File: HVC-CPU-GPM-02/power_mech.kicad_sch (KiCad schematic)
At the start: 24 parts, among them P6 POWER, SW1 RESET, U1 MB8416, U2 74LS373, U3 74LS139, U4 MB8416, U5 RP2C02, U6 RP2A03, U7 74LS368, U8 74LS368

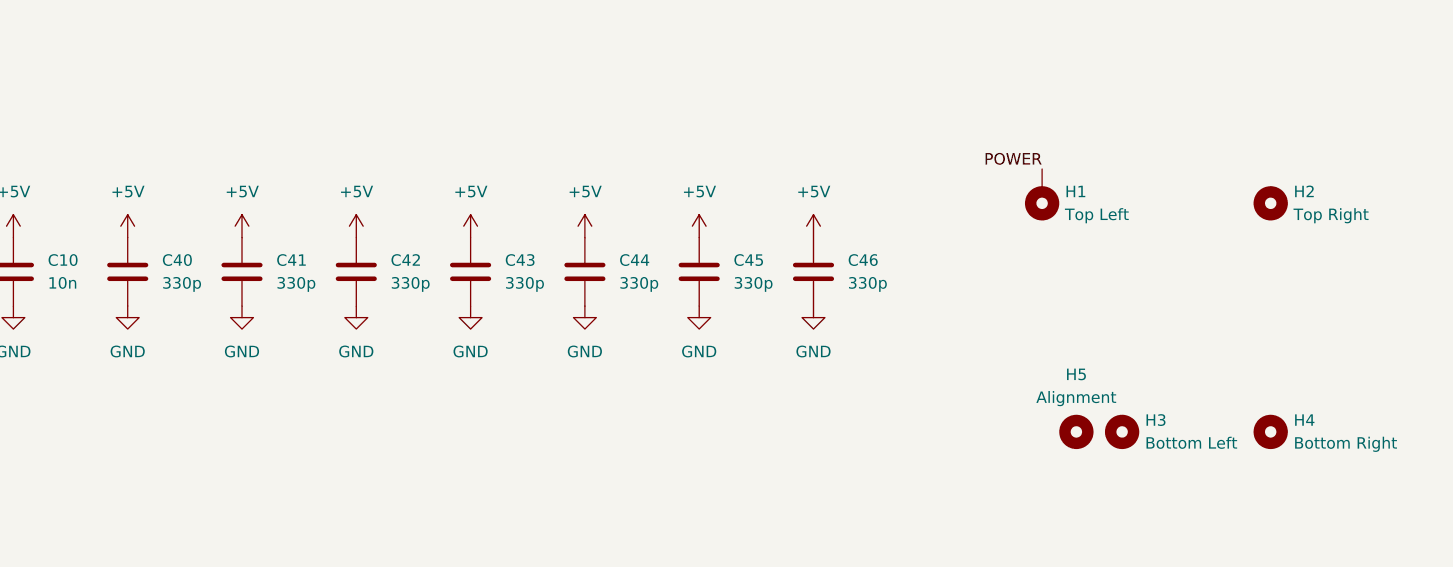
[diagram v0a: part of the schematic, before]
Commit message: Updated PCB and footprints to correct hole and pad sizes
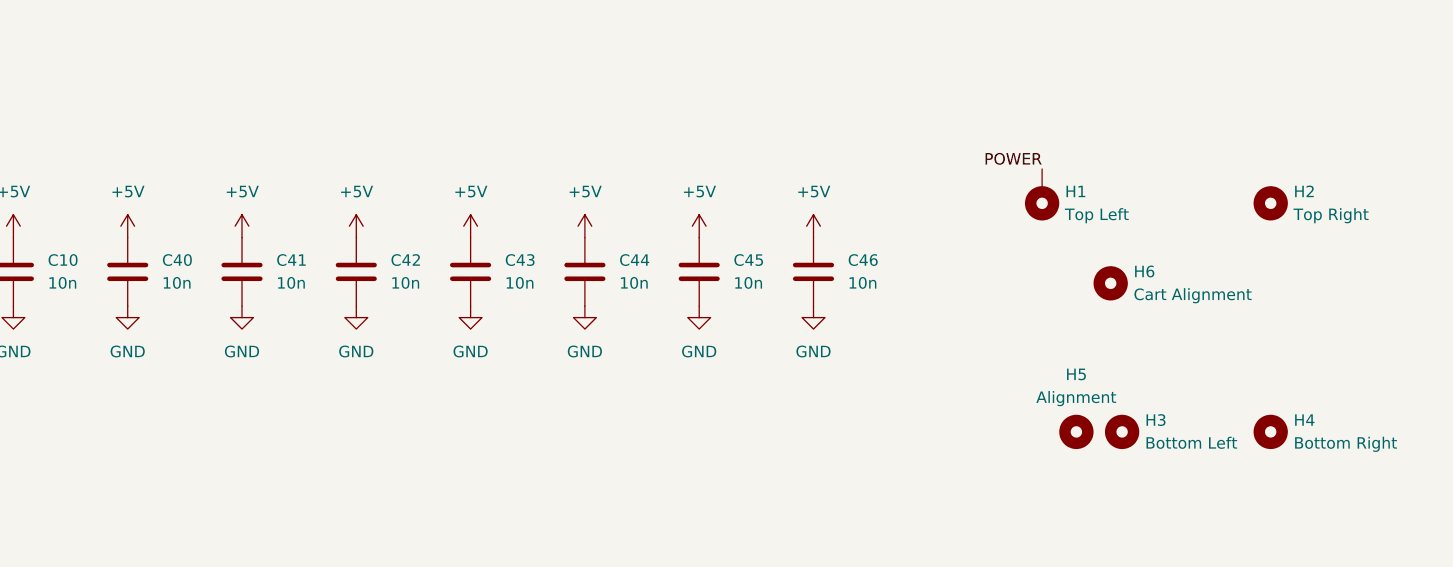
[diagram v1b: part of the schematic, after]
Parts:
- added H6: Cart Alignment, Nintendo:npth_mounting_2.3x3.4mm_nopad, symbol Mechanical:MountingHole
- C40, C41, C42, C43, C44, C45, C46: value 330p -> 10n
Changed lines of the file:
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@@
 			)
 		)
-		(property "Value" "330p"
+		(property "Value" "10n"
 			(at 144.78 97.7899 0)
 			(effects
@@
 			)
 		)
-		(property "Value" "330p"
+		(property "Value" "10n"
 			(at 132.08 97.7899 0)
 			(effects
@@
 			)
 		)
-		(property "Value" "330p"
+		(property "Value" "10n"
 			(at 182.88 97.7899 0)
 			(effects
@@
 			)
 		)
-		(property "Value" "330p"
+		(property "Value" "10n"
 			(at 106.68 97.7899 0)
 			(effects
@@
 			)
 		)
-		(property "Value" "330p"
+		(property "Value" "10n"
 			(at 170.18 97.7899 0)
 			(effects
@@
 				(path "/fb646c2d-03fe-45ba-9ef6-fc3f44aca4b4/26b7c6e0-60f8-49cb-b6c9-8a72e0d0f0d6"
 					(reference "H5")
+					(unit 1)
+				)
+			)
+		)
+	)
+	(symbol
+		(lib_id "Mechanical:MountingHole")
+		(at 212.09 97.79 0)
+		(unit 1)
+		(exclude_from_sim no)
+		(in_bom no)
+		(on_board yes)
+		(dnp no)
+		(fields_autoplaced yes)
+		(property "Reference" "H6"
+			(at 214.63 96.5199 0)
+			(effects
+				(font
+					(size 1.27 1.27)
+				)
+				(justify left)
+			)
+		)
+		(property "Value" "Cart Alignment"
+			(at 214.63 99.0599 0)
+			(effects
+				(font
+					(size 1.27 1.27)
+				)
+				(justify left)
+			)
+		)
+		(property "Footprint" "Nintendo:npth_mounting_2.3x3.4mm_nopad"
+			(at 212.09 97.79 0)
+			(effects
+				(font
+					(size 1.27 1.27)
+				)
+				(hide yes)
+			)
+		)
+		(property "Datasheet" "~"
+			(at 212.09 97.79 0)
+			(effects
+				(font
+					(size 1.27 1.27)
+				)
+				(hide yes)
+			)
+		)
+		(property "Description" "Mounting Hole without connection"
+			(at 212.09 97.79 0)
+			(effects
+				(font
+					(size 1.27 1.27)
+				)
+				(hide yes)
+			)
+		)
+		(instances
+			(project "HVC-CPU-GPM-02"
+				(path "/fb646c2d-03fe-45ba-9ef6-fc3f44aca4b4/26b7c6e0-60f8-49cb-b6c9-8a72e0d0f0d6"
+					(reference "H6")
 					(unit 1)
 				)
@@
 			)
 		)
-		(property "Value" "330p"
+		(property "Value" "10n"
 			(at 157.48 97.7899 0)
 			(effects
@@
 			)
 		)
-		(property "Value" "330p"
+		(property "Value" "10n"
 			(at 119.38 97.7899 0)
 			(effects
